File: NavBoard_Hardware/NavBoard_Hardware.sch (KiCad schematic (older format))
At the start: 59 parts, among them J1 Conn_Coaxial, Q1 BSS138, Q2 BSS138, U2 ATMEGA328P-Project_Library, U3 OKI, U4 OKI, U5 FGPMMOPA6H, Y1 Crystal

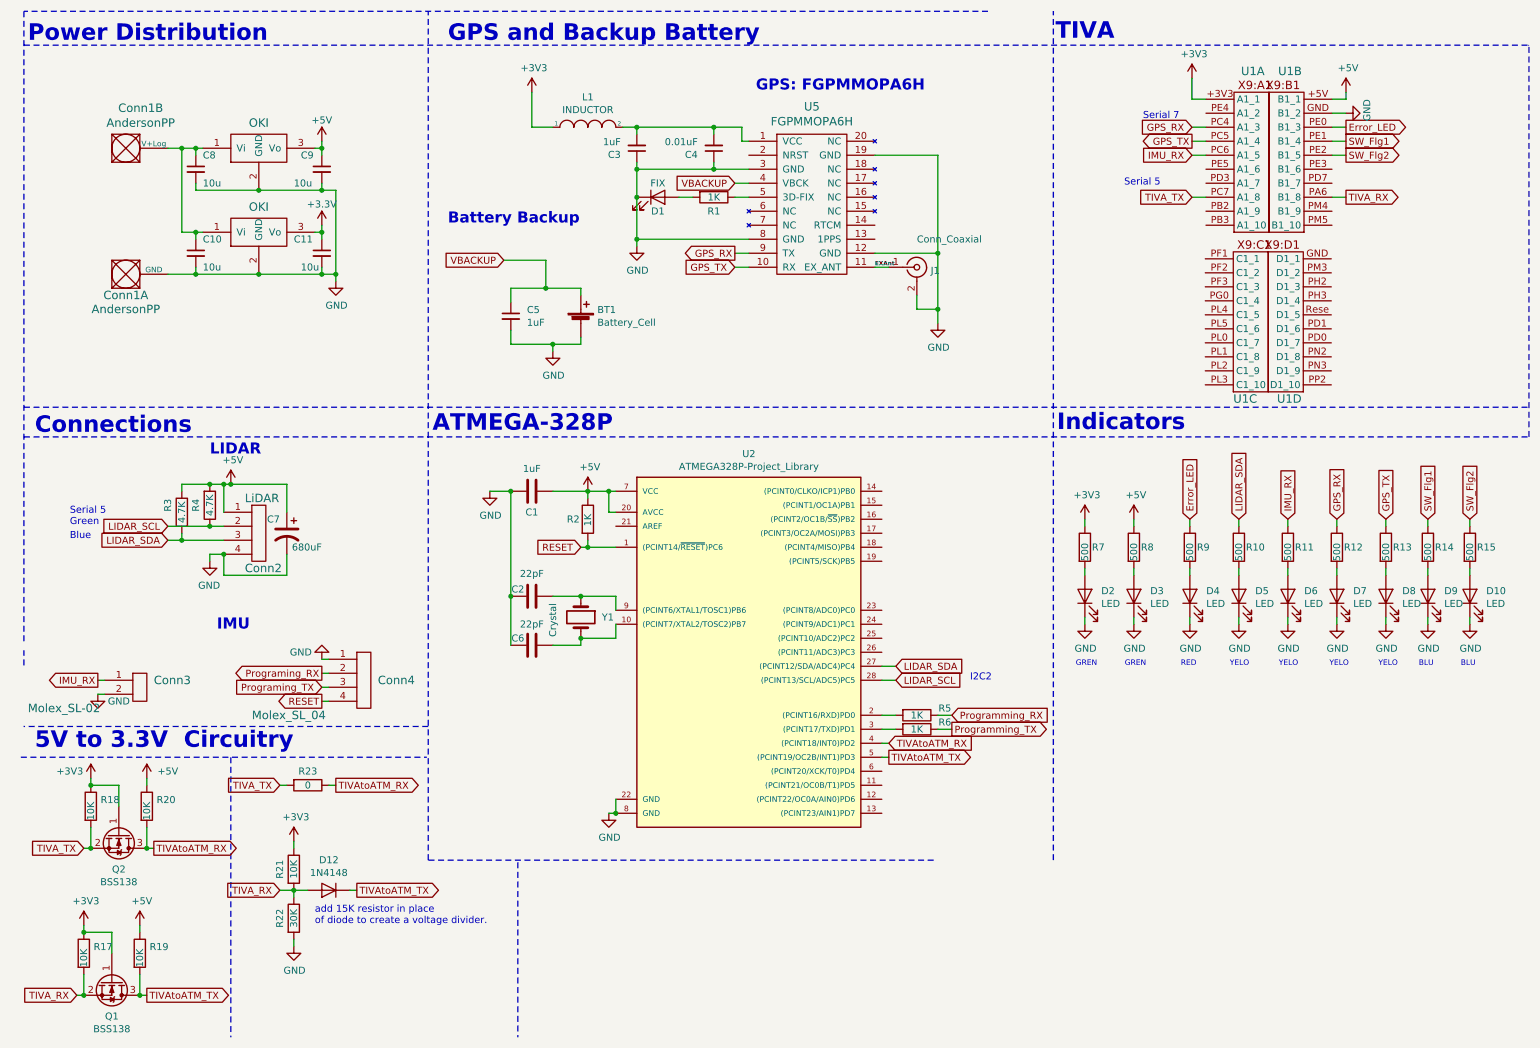
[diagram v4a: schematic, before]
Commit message: fixed direction of signs
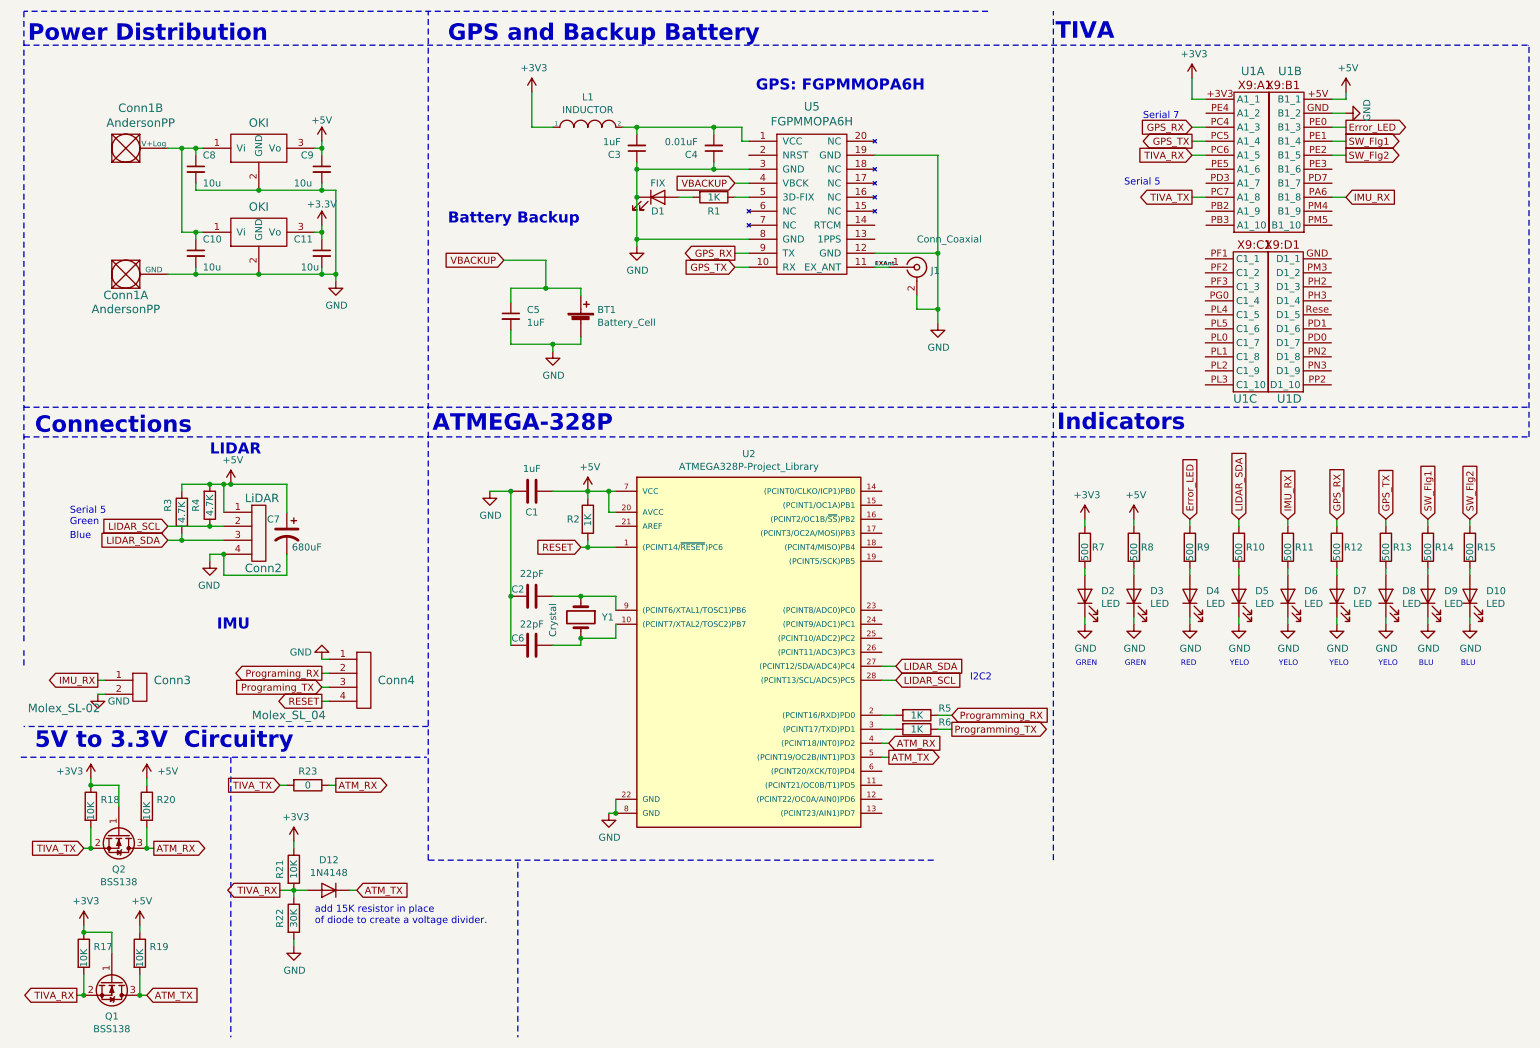
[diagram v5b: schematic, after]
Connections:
- net IMU_RX: now also U1.PA6 (B1_8); no longer U1.PC6 (A1_5)
- net TIVA_RX: now also U1.PC6 (A1_5); no longer U1.PA6 (B1_8)
- net TIVAtoATM_RX renamed ATM_RX
- net TIVAtoATM_TX renamed ATM_TX
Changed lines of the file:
@@
 $EndComp
 Text GLabel 8815 1500 0    50   Input ~ 0
-IMU_RX
+TIVA_RX
 Text GLabel 8815 1300 0    50   Input ~ 0
 GPS_RX
@@
 $EndComp
 Text GLabel 6650 5800 2    50   Output ~ 0
-TIVAtoATM_TX
+ATM_TX
 Text GLabel 6650 5700 2    50   Input ~ 0
-TIVAtoATM_RX
+ATM_RX
 Wire Wire Line
 	6650 5700 6600 5700
 Wire Wire Line
 	6650 5800 6600 5800
-Text GLabel 8815 1800 0    50   Input ~ 0
+Text GLabel 8815 1800 0    50   Output ~ 0
 TIVA_TX
-Text GLabel 9915 1800 2    50   Output ~ 0
-TIVA_RX
+Text GLabel 9915 1800 2    50   Input ~ 0
+IMU_RX
 Wire Wire Line
 	9915 1800 9815 1800
@@
 	900  6450 950  6450
 Text GLabel 1400 6450 2    50   Output ~ 0
-TIVAtoATM_RX
+ATM_RX
 Wire Wire Line
 	1350 6450 1400 6450
@@
 Wire Wire Line
 	1300 7350 1300 7500
-Text GLabel 850  7500 0    50   Input ~ 0
+Text GLabel 850  7500 0    50   Output ~ 0
 TIVA_RX
 Wire Wire Line
 	850  7500 900  7500
-Text GLabel 1350 7500 2    50   Output ~ 0
-TIVAtoATM_TX
+Text GLabel 1350 7500 2    50   Input ~ 0
+ATM_TX
 Wire Wire Line
 	1300 7500 1350 7500
@@
 	2300 6000 2350 6000
 Text GLabel 2700 6000 2    50   Output ~ 0
-TIVAtoATM_RX
+ATM_RX
 Wire Wire Line
 	2650 6000 2700 6000
-Text GLabel 2300 6750 0    50   Input ~ 0
+Text GLabel 2300 6750 0    50   Output ~ 0
 TIVA_RX
 $Comp
@@
 	-1   0    0    1
 $EndComp
-Text GLabel 2850 6750 2    50   Output ~ 0
-TIVAtoATM_TX
+Text GLabel 2850 6750 2    50   Input ~ 0
+ATM_TX
 Wire Wire Line
 	2400 6750 2500 6750

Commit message: nitpicking
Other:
- note added: "03/03/2019\n"
- note added: "2\n"
- note added: "Navigation PCB Rev. 2\n"
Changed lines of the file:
@@
 Wire Wire Line
 	1050 5350 1000 5350
+Text Notes 7350 7500 0    91   ~ 0
+Navigation PCB Rev. 2\n
+Text Notes 8100 7650 0    50   ~ 0
+03/03/2019\n
+Text Notes 10600 7650 0    50   ~ 0
+2\n
 $EndSCHEMATC

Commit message: REV 2
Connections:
- net Programing_RX is gone; now on net Programming_RX: Conn4.2
- net Programing_TX is gone; now on net Programming_TX: Conn4.3
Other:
- note added: "Level Shifter Circuitry"
- note removed: "5V to 3.3V Circuitry"
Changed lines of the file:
@@
 	1000 5250 1050 5250
 Text GLabel 2600 5200 0    50   Output ~ 0
-Programing_RX
+Programming_RX
 Text GLabel 2600 5300 0    50   Input ~ 0
-Programing_TX
+Programming_TX
 Text GLabel 2600 5400 0    50   Output ~ 0
 RESET
@@
 add 15K resistor in place\nof diode to create a voltage divider.\n
 Text Notes 550  5750 0    118  ~ 24
-5V to 3.3V  Circuitry
+Level Shifter Circuitry
 Wire Notes Line
 	450  5800 3350 5800

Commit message: Final touches
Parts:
- removed Conn3: Molex_SL-02, MRDT_Connectors:MOLEX_SL_02_Horizontal, symbol NavBoard_Hardware-rescue:Molex_SL_02-MRDT_Connectors
- added Conn3: Molex_SL_03, MRDT_Connectors:MOLEX_SL_03_Horizontal, symbol NavBoard_Hardware-rescue:Molex_SL_03-MRDT_Connectors
- R2: value 1K -> 10K
- U2: footprint (none) -> Package_DIP:DIP-28_W7.62mm
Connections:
- net +3V3: now also Conn3.1
- net GND: now also Conn3.3
- net IMU_RX: now also Conn3.2
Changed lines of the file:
@@
 F 0 "U2" H 5650 8967 50  0000 C CNN
 F 1 "ATMEGA328P-Project_Library" H 5650 8876 50  0000 C CNN
-F 2 "" H 5600 7600 50  0001 C CIN
+F 2 "Package_DIP:DIP-28_W7.62mm" H 5600 7600 50  0001 C CIN
 F 3 "" H 5600 7600 50  0001 C CNN
 	1    4850 6300
@@
 P 4500 4100
 F 0 "R2" H 4350 4100 50  0000 L CNN
-F 1 "1K" V 4500 4050 50  0000 L CNN
+F 1 "10K" V 4500 4050 50  0000 L CNN
 F 2 "Resistor_SMD:R_0603_1608Metric_Pad1.05x0.95mm_HandSolder" V 4430 4100 50  0001 C CNN
 F 3 "~" H 4500 4100 50  0001 C CNN
@@
 	10800 4800 10800 4850
 $Comp
-L NavBoard_Hardware-rescue:Molex_SL_02-MRDT_Connectors Conn3
-U 1 1 5C7D6386
-P 1250 5400
-F 0 "Conn3" H 1400 5550 60  0000 L CNN
-F 1 "Molex_SL-02" H 500 5350 60  0000 L CNN
-F 2 "MRDT_Connectors:MOLEX_SL_02_Horizontal" H 1250 5400 60  0001 C CNN
-F 3 "" H 1250 5400 60  0001 C CNN
-	1    1250 5400
-	1    0    0    -1
-$EndComp
-$Comp
 L NavBoard_Hardware-rescue:Molex_SL_04-MRDT_Connectors Conn4
 U 1 1 5C7FFA12
@@
 	1    0    0    -1
 $EndComp
-Text GLabel 1000 5250 0    50   Output ~ 0
+Text GLabel 950  5250 0    50   Output ~ 0
 IMU_RX
 Wire Wire Line
-	1000 5250 1050 5250
+	950  5250 1000 5250
 Text GLabel 2600 5200 0    50   Output ~ 0
 Programming_RX
@@
 L power:GND #PWR0127
 U 1 1 5C819482
-P 1000 5350
-F 0 "#PWR0127" H 1000 5100 50  0001 C CNN
-F 1 "GND" H 1150 5300 50  0000 C CNN
-F 2 "" H 1000 5350 50  0001 C CNN
-F 3 "" H 1000 5350 50  0001 C CNN
-	1    1000 5350
+P 950 5350
+F 0 "#PWR0127" H 950 5100 50  0001 C CNN
+F 1 "GND" H 1100 5300 50  0000 C CNN
+F 2 "" H 950 5350 50  0001 C CNN
+F 3 "" H 950 5350 50  0001 C CNN
+	1    950  5350
 	1    0    0    -1
 $EndComp
@@
 	4000 6550 4000 7800
 Wire Wire Line
-	1050 5350 1000 5350
+	1000 5350 950  5350
 Text Notes 7350 7500 0    91   ~ 0
 Navigation PCB Rev. 2\n
@@
 Text Notes 10600 7650 0    50   ~ 0
 2\n
+$Comp
+L NavBoard_Hardware-rescue:Molex_SL_03-MRDT_Connectors Conn3
+U 1 1 5C7DBB4B
+P 1200 5400
+F 0 "Conn3" H 1327 5608 60  0000 L CNN
+F 1 "Molex_SL_03" H 1050 5300 60  0000 L CNN
+F 2 "MRDT_Connectors:MOLEX_SL_03_Horizontal" H 1200 5400 60  0001 C CNN
+F 3 "" H 1200 5400 60  0001 C CNN
+	1    1200 5400
+	1    0    0    -1
+$EndComp
+$Comp
+L power:+3V3 #PWR0129
+U 1 1 5C7F8FA0
+P 950 5150
+F 0 "#PWR0129" H 950 5000 50  0001 C CNN
+F 1 "+3V3" H 965 5323 50  0000 C CNN
+F 2 "" H 950 5150 50  0001 C CNN
+F 3 "" H 950 5150 50  0001 C CNN
+	1    950  5150
+	1    0    0    -1
+$EndComp
+Wire Wire Line
+	1000 5150 950  5150
 $EndSCHEMATC
